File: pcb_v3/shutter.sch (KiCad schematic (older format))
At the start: 39 parts, among them IC1 ATMEGA328P-A, K1 FINDER-36.11, K2 FINDER-36.11, K3 HF49FD, P1 5V_IN, P10 LAMPE, P2 GND5, P3 TX/RX, P4 CONN_01X04, P5 ISP, P6 ANT, P7 NETZ_N, P8 NETZ_L, P9 MOTOR, Q1 BC817, Q2 BC817, Q3 BC817, Y1 8MHZ

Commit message: pcb
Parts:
- removed P10: LAMPE, symbol CONN_01X01
- removed P4: CONN_01X04, symbol CONN_01X04
- added C5: 100nf, Capacitors_SMD:C_0805_HandSoldering, symbol C
- added P4: CONN_01X05, terminal_blocks:RND_Schraubklemme_5pol, symbol CONN_01X05
- C1, C2: footprint (none) -> Capacitors_SMD:C_0805_HandSoldering
- C3, C4: footprint (none) -> Capacitors_SMD:c_elec_5x5.8
- D1, D2, D3: footprint (none) -> Diodes_SMD:MELF_Handsoldering
- F1: footprint (none) -> Fuse_Holders_and_Fuses:Fuseholder5x20_horiz_SemiClosed_Casing10x25mm
- IC1: footprint TQFP32 -> Housings_QFP:TQFP-32_7x7mm_Pitch0.8mm
- K1, K2: footprint Relays_THT:Relay_SPDT_Finder_36.11 -> finder-36:Finder 36.11.9
- K3: footprint Relays_THT:Relay_SPST_HF49FD -> hf49fd:HF49FD
- L1: footprint (none) -> TO_SOT_Packages_SMD:SOT89-3_Housing_Handsoldering
- P1, P2, P6: footprint (none) -> Wire_Pads:SolderWirePad_single_1mmDrill
- P3: footprint (none) -> Pin_Headers:Pin_Header_Straight_1x02
- P5: footprint (none) -> isp:isp
- P7, P8: footprint (none) -> Wire_Pads:SolderWirePad_single_2mmDrill
- P9: footprint (none) -> terminal_blocks:RND_Schraubklemme_2pol
- Q1, Q2, Q3: footprint SOT-23 -> TO_SOT_Packages_SMD:SOT-23
- R1, R10, R2, R3, R4, R5, R6, R7, R8, R9: footprint (none) -> Resistors_SMD:R_0805_HandSoldering
- RF1: footprint (none) -> rfm69:RFM96
- RV1: footprint (none) -> Varistors:RV_Disc_D12_W3.9_P7.5
- Y1: footprint (none) -> Crystals:Crystal_HC49-SD_SMD
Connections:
- net 3.3V: now also C5.1
- net GND: now also C5.2
- net L: now also P4.4 (P4)
- net LAMPE_220V: now reaches K3.14
- net LAMPE_220V: now also P4.5 (P5)
- net at P7.1 (P1), RV1.1: now also P4.1 (P1), P4.2 (P2), P4.3 (P3)

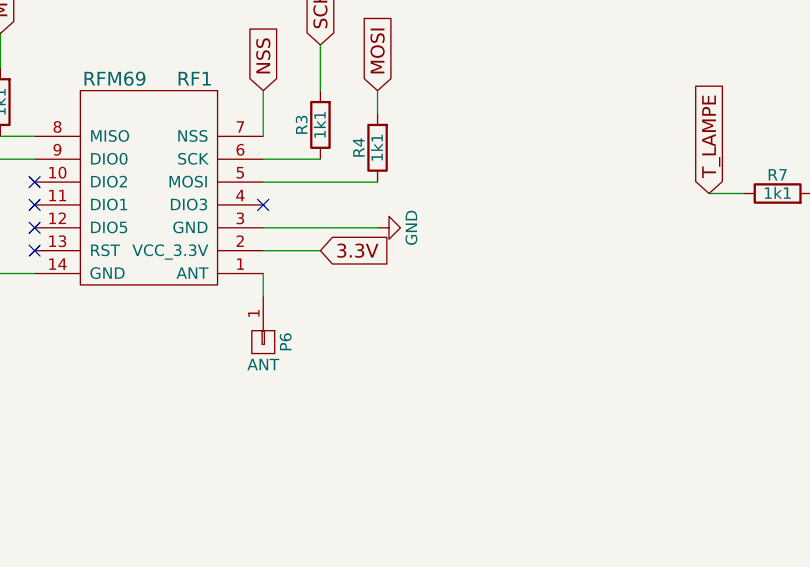
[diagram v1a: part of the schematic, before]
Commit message: added jumper for power rfm69
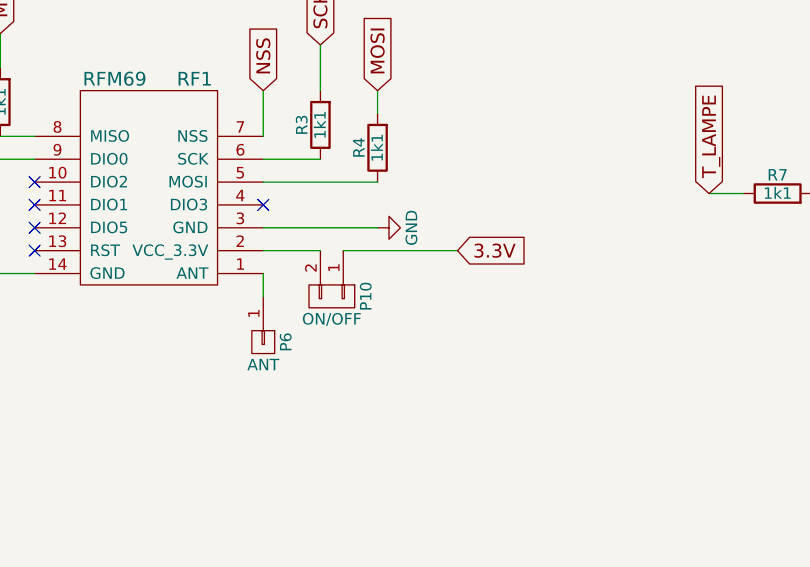
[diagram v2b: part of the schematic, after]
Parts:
- added P10: ON/OFF, Pin_Headers:Pin_Header_Straight_1x02, symbol CONN_01X02
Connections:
- net 3.3V: now also P10.1 (P1); no longer RF1.2 (VCC_3.3V)
- new net: P10.2 (P2), RF1.2 (VCC_3.3V)
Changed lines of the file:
@@
 	1    0    0    -1
 $EndComp
-Text GLabel 6750 4450 2    60   Input ~ 0
+Text GLabel 7350 4450 2    60   Input ~ 0
 3.3V
-Wire Wire Line
-	6750 4450 6500 4450
 $Comp
 L CONN_01X01 P6
@@
 	4750 6650 4750 6850
 Connection ~ 4750 6750
+$Comp
+L CONN_01X02 P10
+U 1 1 5A89A40D
+P 6800 4650
+F 0 "P10" H 6800 4800 50  0000 C CNN
+F 1 "ON/OFF" V 6900 4650 50  0000 C CNN
+F 2 "Pin_Headers:Pin_Header_Straight_1x02" H 6800 4650 50  0001 C CNN
+F 3 "" H 6800 4650 50  0000 C CNN
+	1    6800 4650
+	0    1    1    0
+$EndComp
+Wire Wire Line
+	6500 4450 6750 4450
+Wire Wire Line
+	6850 4450 7350 4450
 $EndSCHEMATC

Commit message: updated schema
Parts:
- Q1, Q2, Q3: footprint TO_SOT_Packages_SMD:SOT-23 -> SOT-23
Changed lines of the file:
@@
 F 0 "Q3" H 9550 4275 50  0000 L CNN
 F 1 "BC817" H 9550 4200 50  0000 L CNN
-F 2 "TO_SOT_Packages_SMD:SOT-23" H 9550 4125 50  0000 L CIN
+F 2 "SOT-23" H 9550 4125 50  0000 L CIN
 F 3 "" H 9350 4200 50  0000 L CNN
 	1    9350 4200
@@
 F 0 "Q2" H 9300 2875 50  0000 L CNN
 F 1 "BC817" H 9300 2800 50  0000 L CNN
-F 2 "TO_SOT_Packages_SMD:SOT-23" H 9300 2725 50  0000 L CIN
+F 2 "SOT-23" H 9300 2725 50  0000 L CIN
 F 3 "" H 9100 2800 50  0000 L CNN
 	1    9100 2800
@@
 F 0 "Q1" H 9050 1525 50  0000 L CNN
 F 1 "BC817" H 9050 1450 50  0000 L CNN
-F 2 "TO_SOT_Packages_SMD:SOT-23" H 9050 1375 50  0000 L CIN
+F 2 "SOT-23" H 9050 1375 50  0000 L CIN
 F 3 "" H 8850 1450 50  0000 L CNN
 	1    8850 1450
